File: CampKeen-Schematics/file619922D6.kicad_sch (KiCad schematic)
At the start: 64 parts, among them IC11 LTV-814, IC12 LTV-814, Q20 2N7000, Q21 2N7000, Q22 2N7000, Q23 2N7000, Q24 2N7000, Q25 2N7000, Q26 2N7000, Q27 2N7000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

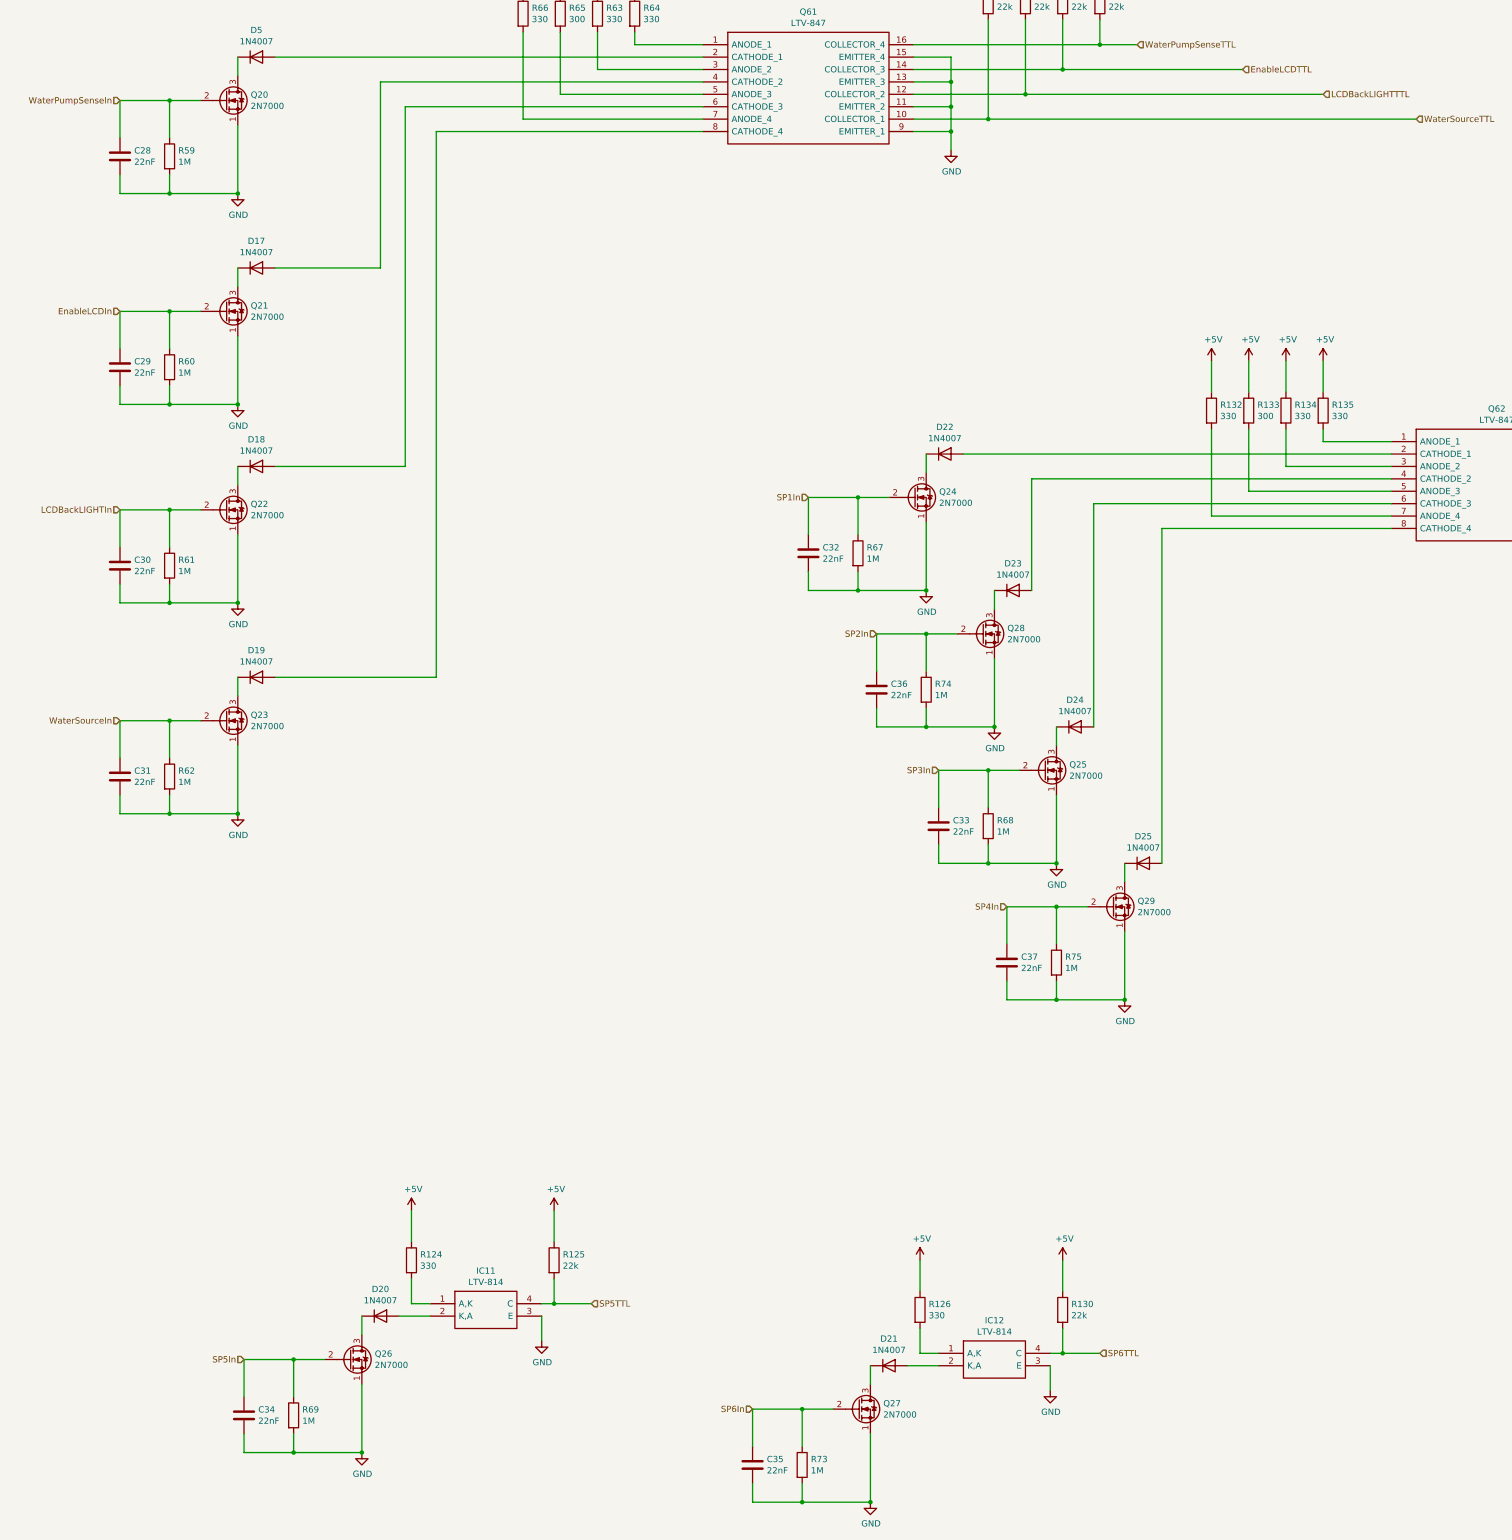
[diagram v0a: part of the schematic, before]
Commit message: removed from schematic - lcd backlight enable - lcd backlight out - moving gpio around to get free serial pins.
starting to remove the parts from the PCB
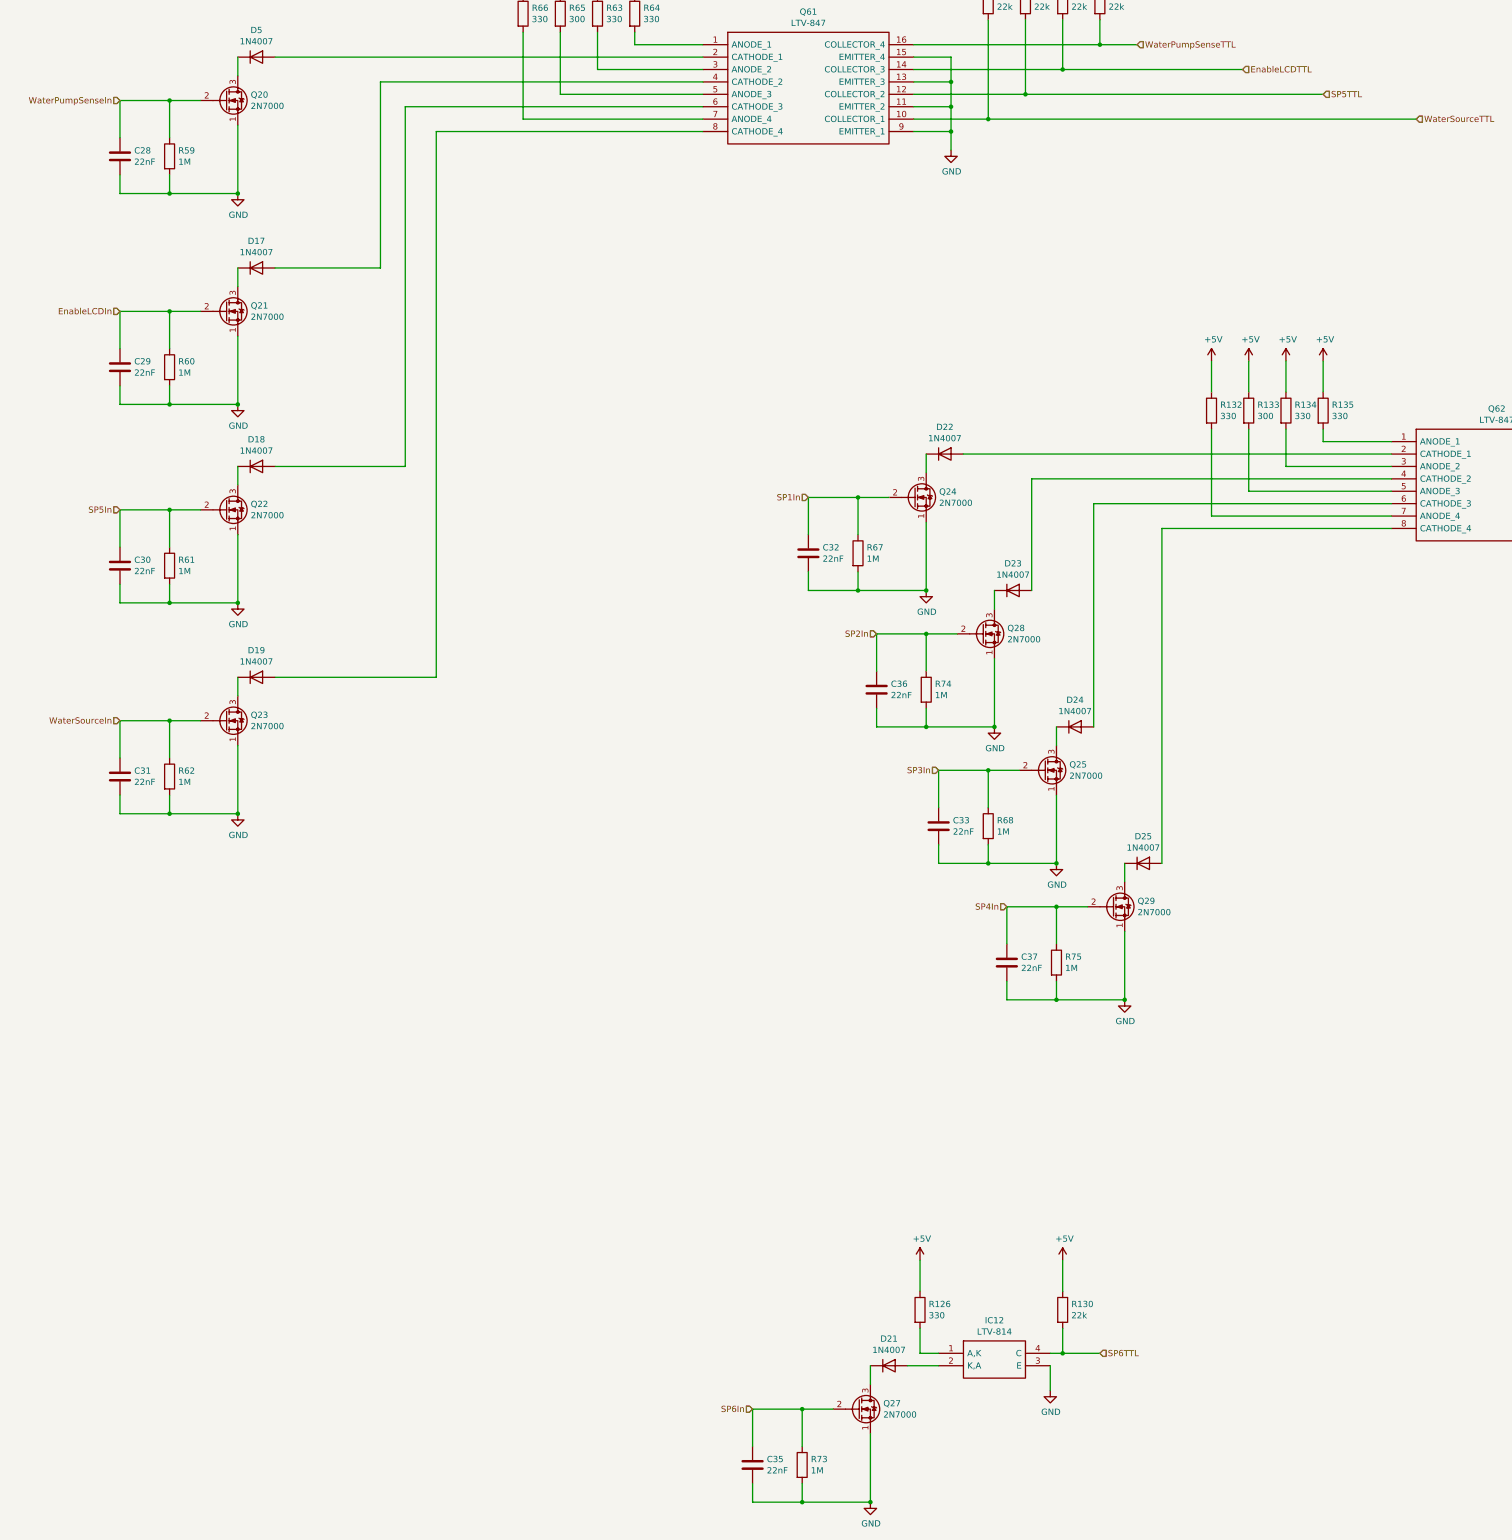
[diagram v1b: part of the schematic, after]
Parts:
- removed C34: 22nF, Capacitor_THT:C_Disc_D4.7mm_W2.5mm_P5.00mm, symbol Device:C
- removed D20: 1N4007, Diode_THT:D_DO-41_SOD81_P10.16mm_Horizontal, symbol Diode:1N4007
- removed IC11: LTV-814, DIP762W60P254L460H450Q4N, symbol SamacSys_Parts:LTV-814
- removed Q26: 2N7000, Package_TO_SOT_THT:TO-92_Inline, symbol Transistor_FET:2N7000
- removed R124: 330, Resistor_THT:R_Axial_DIN0207_L6.3mm_D2.5mm_P2.54mm_Vertical, symbol Device:R
- removed R125: 22k, Resistor_THT:R_Axial_DIN0207_L6.3mm_D2.5mm_P2.54mm_Vertical, symbol Device:R
- removed R69: 1M, Resistor_THT:R_Axial_DIN0207_L6.3mm_D2.5mm_P2.54mm_Vertical, symbol Device:R
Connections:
- net LCDBackLIGHTIn is gone; now on net SP5In: C30.1, Q22.2 (G), R61.1
- net LCDBackLIGHTTTL is gone; now on net SP5TTL: Q61.12 (COLLECTOR_2), R128.2

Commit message: working on input protection.
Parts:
- IC12: footprint DIP762W60P254L460H450Q4N -> SamacSys_Parts:DIP762W60P254L460H450Q4N
- Q61, Q62: footprint DIP762W60P254L1984H450Q16N -> SamacSys_Parts:DIP762W60P254L1984H450Q16N
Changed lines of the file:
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@@
     (property "Reference" "Q61" (id 0) (at 184.15 58.039 0))
     (property "Value" "LTV-847" (id 1) (at 184.15 60.3504 0))
-    (property "Footprint" "DIP762W60P254L1984H450Q16N" (id 2) (at 201.93 62.23 0)
+    (property "Footprint" "SamacSys_Parts:DIP762W60P254L1984H450Q16N" (id 2) (at 201.93 62.23 0)
       (effects (font (size 1.27 1.27)) (justify left) hide)
     )
@@
     (property "Reference" "Q62" (id 0) (at 325.12 139.319 0))
     (property "Value" "LTV-847" (id 1) (at 325.12 141.6304 0))
-    (property "Footprint" "DIP762W60P254L1984H450Q16N" (id 2) (at 342.9 143.51 0)
+    (property "Footprint" "SamacSys_Parts:DIP762W60P254L1984H450Q16N" (id 2) (at 342.9 143.51 0)
       (effects (font (size 1.27 1.27)) (justify left) hide)
     )
@@
     (property "Reference" "IC12" (id 0) (at 222.25 326.009 0))
     (property "Value" "LTV-814" (id 1) (at 222.25 328.3204 0))
-    (property "Footprint" "DIP762W60P254L460H450Q4N" (id 2) (at 229.87 330.2 0)
-      (effects (font (size 1.27 1.27)) (justify left) hide)
-    )
+    (property "Footprint" "SamacSys_Parts:DIP762W60P254L460H450Q4N" (id 2) (at 229.87 330.2 0)
+      (effects (font (size 1.27 1.27)) (justify left) hide)
+    )
